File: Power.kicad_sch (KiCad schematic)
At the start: 28 parts, among them IC4 NCV8165ML330TCG, IC6 CYPD3177-24LQXQ, J1 USB_C_Receptacle_PowerOnly_6P, Q1 IRF9358TRPBF, Q2 BSL308PEH6327XTSA1, Q6 IRF9358TRPBF

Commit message: cell changes and fixes
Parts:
- added R68: R_US, symbol Device:R_US
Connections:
- net 20V to 5V Buck/BUCK_VOUT: now also R68.2
- net GND: now also R68.1
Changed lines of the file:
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@@
 	)
 	(junction
+		(at 22.225 91.44)
+		(diameter 0)
+		(color 0 0 0 0)
+	)
+	(junction
 		(at 107.95 82.55)
 		(diameter 0)
@@
 	(wire
 		(pts
+			(xy 22.225 91.44) (xy 18.415 91.44)
+		)
+		(stroke
+			(width 0)
+			(type default)
+		)
+	)
+	(wire
+		(pts
 			(xy 107.95 92.71) (xy 107.95 91.44)
 		)
@@
 	(wire
 		(pts
+			(xy 18.415 91.44) (xy 18.415 93.345)
+		)
+		(stroke
+			(width 0)
+			(type default)
+		)
+	)
+	(wire
+		(pts
 			(xy 189.23 52.07) (xy 189.23 59.69)
 		)
@@
 					(unit 1)
 				)
+			)
+		)
+	)
+	(symbol
+		(lib_id "power:GND")
+		(at 18.415 100.965 0)
+		(unit 1)
+		(exclude_from_sim no)
+		(in_bom yes)
+		(on_board yes)
+		(dnp no)
+		(fields_autoplaced yes)
+		(property "Reference" "#PWR092"
+			(at 18.415 107.315 0)
+			(effects
+				(font
+					(size 1.27 1.27)
+				)
+				(hide yes)
+			)
+		)
+		(property "Value" "GND"
+			(at 18.415 105.41 0)
+			(effects
+				(font
+					(size 1.27 1.27)
+				)
+			)
+		)
+		(property "Footprint" ""
+			(at 18.415 100.965 0)
+			(effects
+				(font
+					(size 1.27 1.27)
+				)
+				(hide yes)
+			)
+		)
+		(property "Datasheet" ""
+			(at 18.415 100.965 0)
+			(effects
+				(font
+					(size 1.27 1.27)
+				)
+				(hide yes)
+			)
+		)
+		(property "Description" "Power symbol creates a global label with name \"GND\" , ground"
+			(at 18.415 100.965 0)
+			(effects
+				(font
+					(size 1.27 1.27)
+				)
+				(hide yes)
+			)
+		)
+		(pin "1"
+		)
+		(instances
+			(project ""
+				(path "/8cf78a1b-eb7a-4166-aa75-ad898a030304/02e804c2-1162-421a-8f6e-0436cbda7935"
+					(reference "#PWR092")
+					(unit 1)
+				)
+			)
+		)
+	)
+	(symbol
+		(lib_id "Device:R_US")
+		(at 18.415 97.155 180)
+		(unit 1)
+		(exclude_from_sim no)
+		(in_bom yes)
+		(on_board yes)
+		(dnp yes)
+		(fields_autoplaced yes)
+		(property "Reference" "R68"
+			(at 20.32 95.8849 0)
+			(effects
+				(font
+					(size 1.27 1.27)
+				)
+				(justify right)
+			)
+		)
+		(property "Value" "R_US"
+			(at 20.32 98.4249 0)
+			(effects
+				(font
+					(size 1.27 1.27)
+				)
+				(justify right)
+			)
+		)
+		(property "Footprint" ""
+			(at 17.399 96.901 90)
+			(effects
+				(font
+					(size 1.27 1.27)
+				)
+				(hide yes)
+			)
+		)
+		(property "Datasheet" "~"
+			(at 18.415 97.155 0)
+			(effects
+				(font
+					(size 1.27 1.27)
+				)
+				(hide yes)
+			)
+		)
+		(property "Description" "Resistor, US symbol"
+			(at 18.415 97.155 0)
+			(effects
+				(font
+					(size 1.27 1.27)
+				)
+				(hide yes)
+			)
+		)
+		(pin "1"
+		)
+		(pin "2"
+		)
+		(instances
+			(project "Cell-Characterization-Board"
+				(path "/8cf78a1b-eb7a-4166-aa75-ad898a030304/02e804c2-1162-421a-8f6e-0436cbda7935"
+					(reference "R68")
+					(unit 1)
+				)

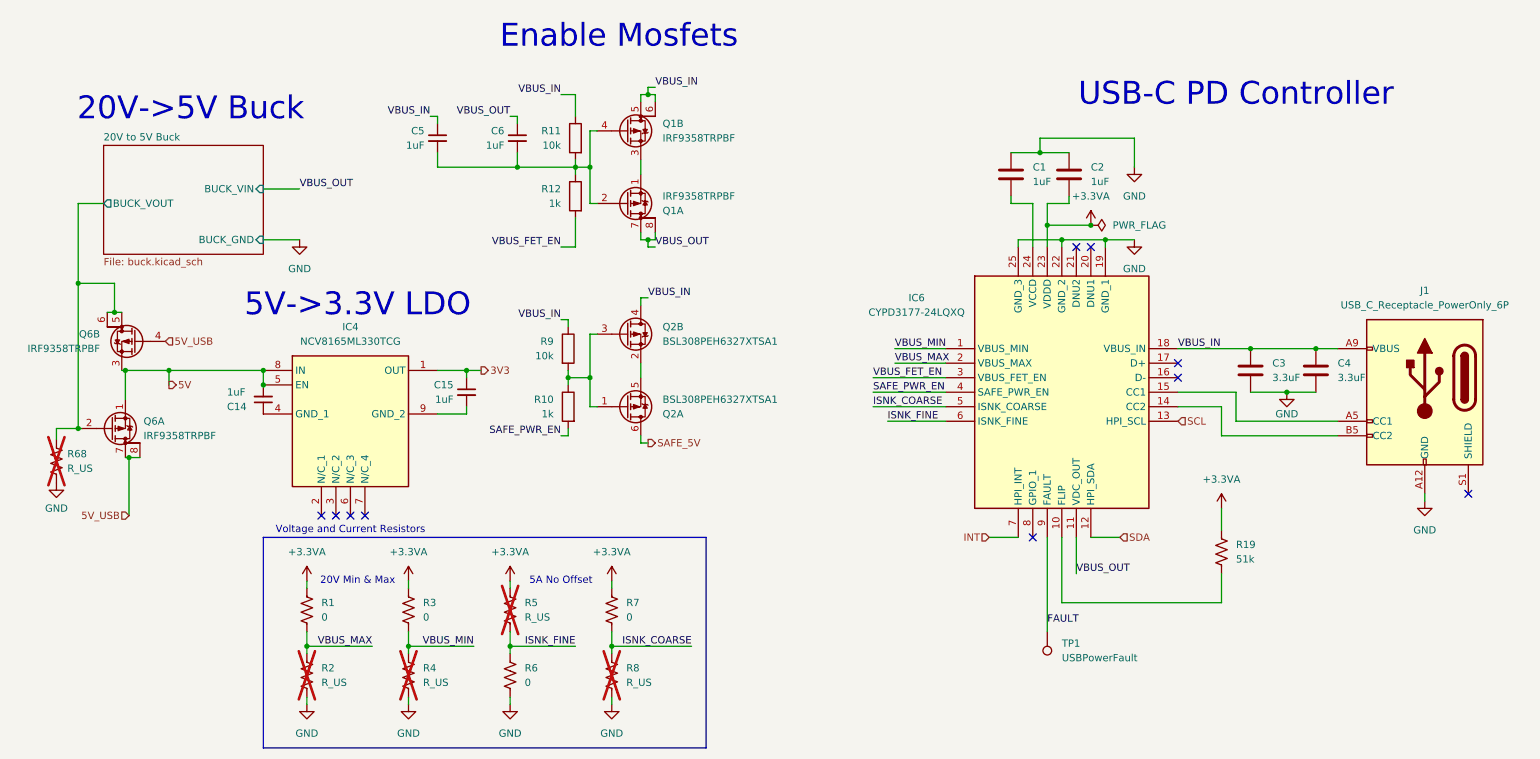
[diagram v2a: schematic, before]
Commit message: Updated current control loop hardware
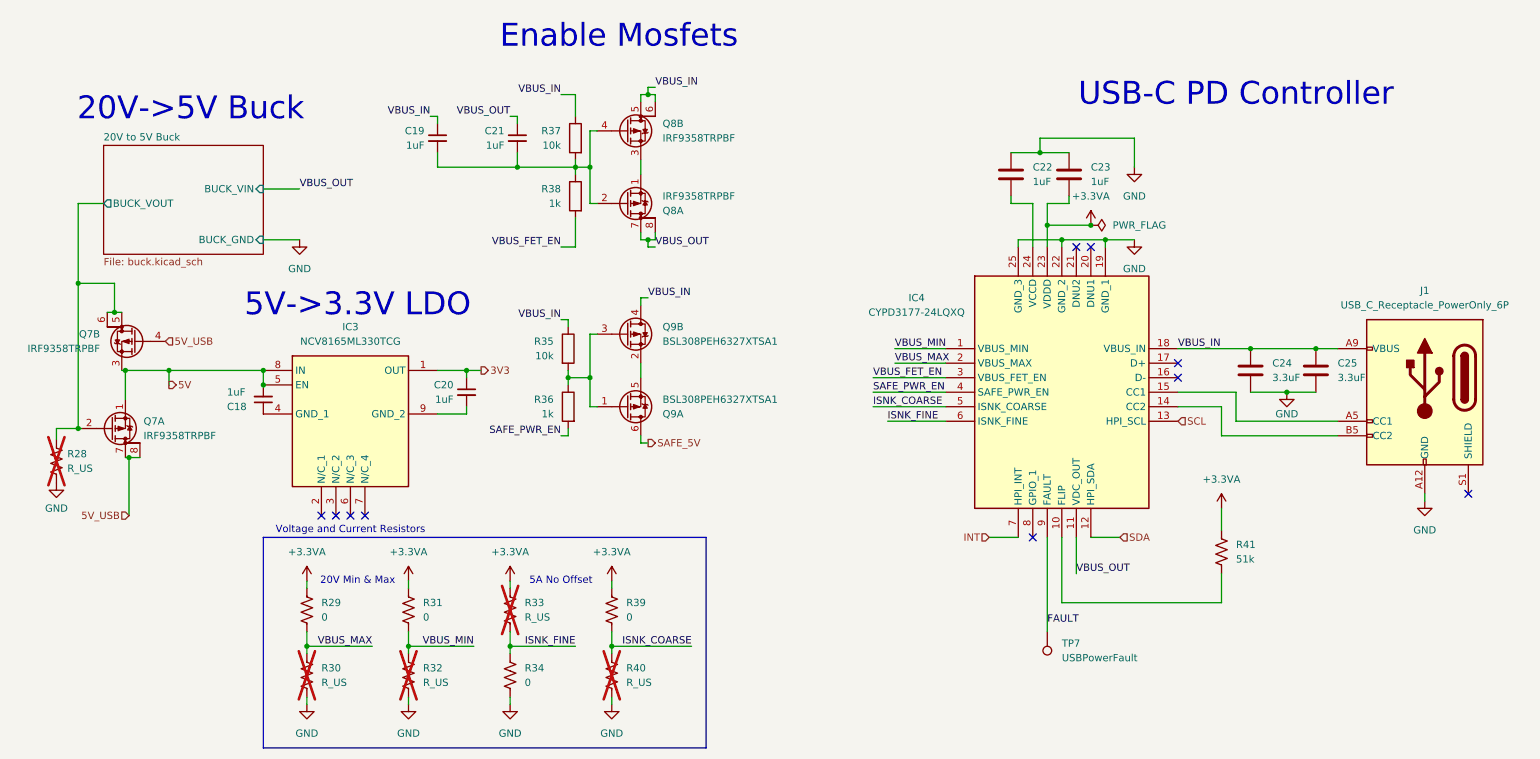
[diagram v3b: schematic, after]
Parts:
- renumbered C14 to C18, C5 to C19, C15 to C20, C6 to C21, C1 to C22, C2 to C23, C3 to C24, C4 to C25, IC4 to IC3, IC6 to IC4, Q6 to Q7, Q1 to Q8, Q2 to Q9, R68 to R28, R1 to R29, R2 to R30, R3 to R31, R4 to R32, R5 to R33, R6 to R34, R9 to R35, R10 to R36, R11 to R37, R12 to R38, R7 to R39, R8 to R40, R19 to R41, TP1 to TP7

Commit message: footprints and components for buck and power
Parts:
- C22, C23, C24, C25: footprint (none) -> Capacitor_SMD:C_0805_2012Metric
- J1: footprint (none) -> Connector_USB:USB_C_Receptacle_HCTL_HC-TYPE-C-16P-01A
- R28, R29, R30, R31, R32, R33, R34, R39, R40, R41: footprint (none) -> Resistor_SMD:R_0805_2012Metric
- TP7: footprint (none) -> UTSVT_Special:TestPoint_HEX_3mmID
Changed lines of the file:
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@@
 			)
 		)
-		(property "Footprint" ""
+		(property "Footprint" "UTSVT_Special:TestPoint_HEX_3mmID"
 			(at 186.69 127 0)
 			(effects
@@
 			)
 		)
-		(property "Footprint" ""
+		(property "Footprint" "Resistor_SMD:R_0805_2012Metric"
 			(at 223.266 113.284 90)
 			(effects
@@
 			)
 		)
-		(property "Footprint" ""
+		(property "Footprint" "Resistor_SMD:R_0805_2012Metric"
 			(at 63.246 123.444 90)
 			(effects
@@
 			)
 		)
-		(property "Footprint" ""
+		(property "Footprint" "Resistor_SMD:R_0805_2012Metric"
 			(at 63.246 134.874 90)
 			(effects
@@
 			)
 		)
-		(property "Footprint" ""
+		(property "Footprint" "Resistor_SMD:R_0805_2012Metric"
 			(at 81.026 134.874 90)
 			(effects
@@
 			)
 		)
-		(property "Footprint" ""
+		(property "Footprint" "Capacitor_SMD:C_0805_2012Metric"
 			(at 228.2952 85.09 0)
 			(effects
@@
 			)
 		)
-		(property "Footprint" ""
+		(property "Footprint" "Resistor_SMD:R_0805_2012Metric"
 			(at 17.399 96.901 90)
 			(effects
@@
 			)
 		)
-		(property "Footprint" ""
+		(property "Footprint" "Capacitor_SMD:C_0805_2012Metric"
 			(at 239.7252 85.09 0)
 			(effects
@@
 			)
 		)
-		(property "Footprint" ""
+		(property "Footprint" "Capacitor_SMD:C_0805_2012Metric"
 			(at 184.4548 43.18 0)
 			(effects
@@
 			)
 		)
-		(property "Footprint" ""
+		(property "Footprint" "Resistor_SMD:R_0805_2012Metric"
 			(at 98.806 123.444 90)
 			(effects
@@
 			)
 		)
-		(property "Footprint" ""
+		(property "Footprint" "Resistor_SMD:R_0805_2012Metric"
 			(at 116.586 123.444 90)
 			(effects
@@
 			)
 		)
-		(property "Footprint" ""
+		(property "Footprint" "Resistor_SMD:R_0805_2012Metric"
 			(at 98.806 134.874 90)
 			(effects
@@
 			)
 		)
-		(property "Footprint" ""
+		(property "Footprint" "Capacitor_SMD:C_0805_2012Metric"
 			(at 196.5452 50.8 0)
 			(effects
@@
 			)
 		)
-		(property "Footprint" ""
+		(property "Footprint" "Resistor_SMD:R_0805_2012Metric"
 			(at 81.026 123.444 90)
 			(effects
@@
 			)
 		)
-		(property "Footprint" ""
+		(property "Footprint" "Resistor_SMD:R_0805_2012Metric"
 			(at 116.586 134.874 90)
 			(effects
@@
 			)
 		)
-		(property "Footprint" ""
+		(property "Footprint" "Connector_USB:USB_C_Receptacle_HCTL_HC-TYPE-C-16P-01A"
 			(at 254 82.55 0)
 			(effects

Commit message: updated symbol for screen and added testpoints
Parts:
- added TP10: VBUS_IN, UTSVT_Special:TestPoint_HEX_3mmID, symbol Connector:TestPoint
- added TP11: USBC_GND, UTSVT_Special:TestPoint_HEX_3mmID, symbol Connector:TestPoint
- added TP12: VBUS_OUT, UTSVT_Special:TestPoint_HEX_3mmID, symbol Connector:TestPoint
- added TP13: BUCK_VOUT, UTSVT_Special:TestPoint_HEX_3mmID, symbol Connector:TestPoint
- added TP14: 5V, UTSVT_Special:TestPoint_HEX_3mmID, symbol Connector:TestPoint
- added TP15: SAFE_5V, UTSVT_Special:TestPoint_HEX_3mmID, symbol Connector:TestPoint
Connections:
- net 20V to 5V Buck/BUCK_VOUT: now also TP13.1
- net 5V: now also TP14.1
- net GND: now also TP11.1
- net SAFE_5V: now also TP15.1
- net VBUS_IN: now also TP10.1
- net VBUS_OUT: now also TP12.1
